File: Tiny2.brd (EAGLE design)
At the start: 30.1 x 64.9 mm, 13 parts

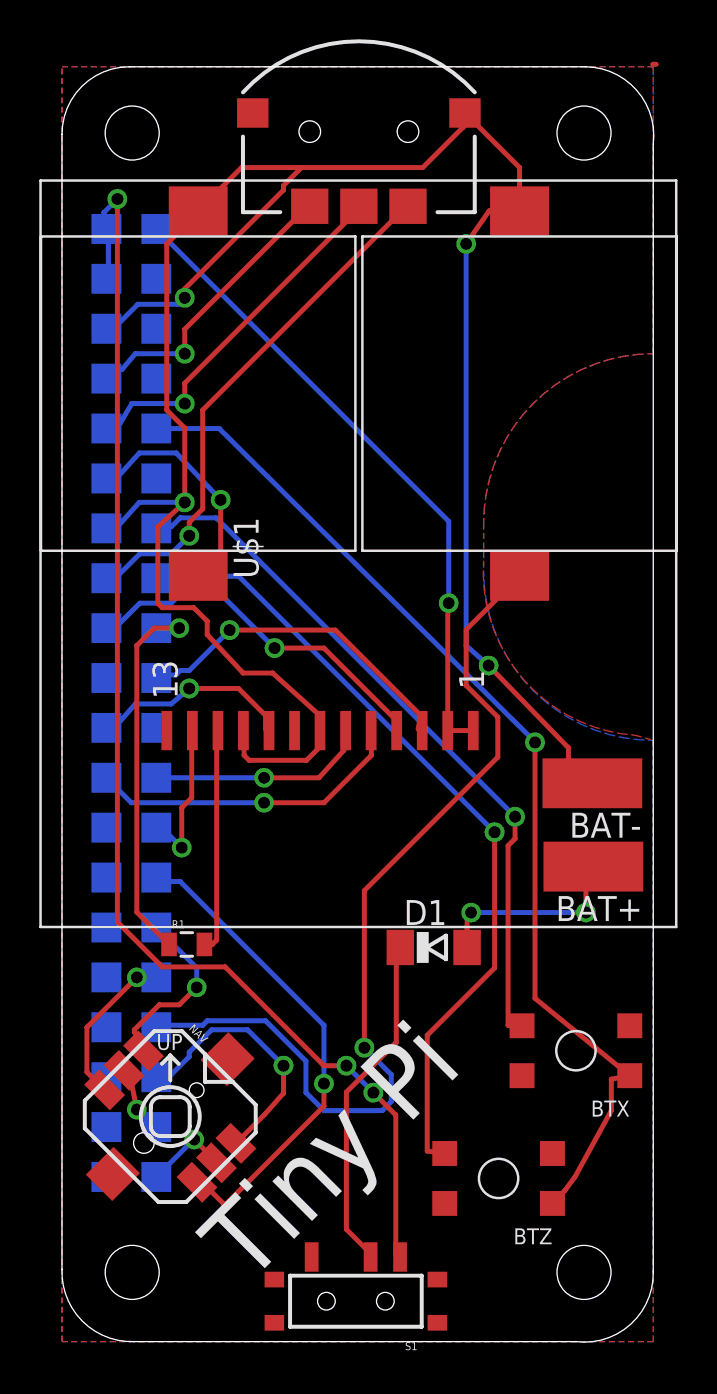
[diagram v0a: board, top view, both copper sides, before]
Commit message: removed diode, cleaned up some vias inside the header section
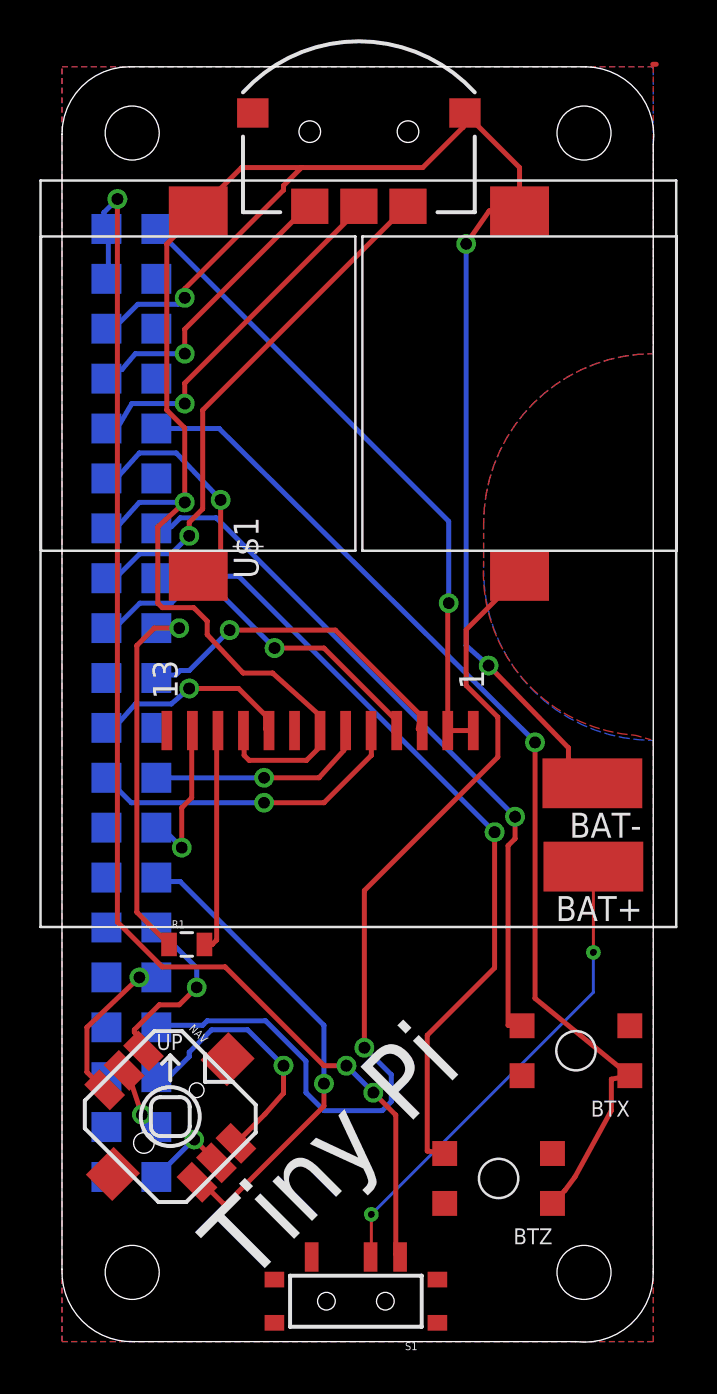
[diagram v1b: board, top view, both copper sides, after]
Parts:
- removed D1: PMLL4150, diode:SOD80C
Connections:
- removed net N$21: D1.C, S1.P
- net N$20: now also S1.P; no longer D1.A
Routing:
- net N$21: track 17.4 -> 0.00 mm
- net N$20: track 10.2 -> 24.6 mm
- net N$4: track 3.49 -> 4.12 mm
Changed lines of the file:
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@@
 <?xml version="1.0" encoding="utf-8"?>
 <!DOCTYPE eagle SYSTEM "eagle.dtd">
-<eagle version="8.1.0">
+<eagle version="8.3.2">
 <drawing>
 <settings>
 <setting alwaysvectorfont="no"/>
+<setting keepoldvectorfont="yes"/>
 <setting verticaltext="up"/>
 </settings>
@@
 <attribute name="PROD_ID" value="SWCH-08301" x="17.78" y="62.865" size="1.778" layer="27" display="off"/>
 </element>
-<element name="D1" library="diode" package="SOD80C" value="PMLL4150" x="21.59" y="21.336"/>
 </elements>
 <signals>
@@
 <contactref element="PI1" pad="37"/>
 <wire x1="7.4676" y1="12.192" x2="6.477" y2="13.0556" width="0.254" layer="16"/>
-<via x="6.477" y="13.081" extent="1-16" drill="0.6" alwaysstop="yes"/>
-<wire x1="6.477" y1="13.081" x2="6.223" y2="14.351" width="0.254" layer="1"/>
+<via x="6.731" y="12.827" extent="1-16" drill="0.6" alwaysstop="yes"/>
+<wire x1="6.731" y1="12.827" x2="6.223" y2="14.351" width="0.254" layer="1"/>
 <wire x1="6.223" y1="14.351" x2="5.878471875" y2="15.076528125" width="0.254" layer="1"/>
 <wire x1="5.878471875" y1="15.076528125" x2="5.82766875" y2="15.076528125" width="0.254" layer="1"/>
-<wire x1="6.477" y1="13.0556" x2="6.477" y2="13.081" width="0.254" layer="16"/>
+<wire x1="6.477" y1="13.0556" x2="6.731" y2="12.827" width="0.254" layer="16"/>
 </signal>
 <signal name="N$5">
@@
 <wire x1="4.83771875" y1="14.086578125" x2="3.937" y2="14.987296875" width="0.254" layer="1"/>
 <wire x1="3.937" y1="14.987296875" x2="3.937" y2="17.272" width="0.254" layer="1"/>
-<wire x1="3.937" y1="17.272" x2="6.477" y2="19.812" width="0.254" layer="1"/>
-<via x="6.477" y="19.812" extent="1-16" drill="0.6"/>
-<wire x1="6.477" y1="19.812" x2="7.4676" y2="19.812" width="0.254" layer="16"/>
+<wire x1="3.937" y1="17.272" x2="6.604" y2="19.812" width="0.254" layer="1"/>
+<via x="6.604" y="19.812" extent="1-16" drill="0.6"/>
+<wire x1="6.604" y1="19.812" x2="7.4676" y2="19.812" width="0.254" layer="16"/>
 </signal>
 <signal name="N$9">
@@
 <signal name="N$20">
 <contactref element="BAT+" pad="1"/>
-<contactref element="D1" pad="A"/>
-<wire x1="29.718" y1="25.4508" x2="29.337" y2="25.0698" width="0.254" layer="1"/>
-<wire x1="29.337" y1="25.0698" x2="29.337" y2="23.114" width="0.254" layer="1"/>
-<via x="29.337" y="23.114" extent="1-16" drill="0.6"/>
-<wire x1="29.337" y1="23.114" x2="23.495" y2="23.114" width="0.254" layer="16"/>
-<via x="23.495" y="23.114" extent="1-16" drill="0.6"/>
-<wire x1="23.495" y1="23.114" x2="23.29" y2="22.909" width="0.254" layer="1"/>
-<wire x1="23.29" y1="22.909" x2="23.29" y2="21.336" width="0.254" layer="1"/>
-</signal>
-<signal name="N$21">
-<contactref element="D1" pad="C"/>
 <contactref element="S1" pad="P"/>
-<wire x1="19.89" y1="21.336" x2="19.685" y2="20.623" width="0.254" layer="1"/>
-<wire x1="19.685" y1="20.623" x2="19.685" y2="16.51" width="0.254" layer="1"/>
-<wire x1="19.685" y1="16.51" x2="17.145" y2="13.97" width="0.254" layer="1"/>
-<wire x1="17.145" y1="13.97" x2="17.145" y2="6.985" width="0.254" layer="1"/>
-<wire x1="17.145" y1="6.985" x2="18.3776" y2="5.7524" width="0.254" layer="1"/>
-<wire x1="18.3776" y1="5.7524" x2="18.3776" y2="5.5774" width="0.254" layer="1"/>
+<wire x1="29.718" y1="25.4508" x2="29.718" y2="21.082" width="0.1524" layer="1"/>
+<via x="29.718" y="21.082" extent="1-16" drill="0.35"/>
+<wire x1="29.718" y1="21.082" x2="29.718" y2="19.05" width="0.1524" layer="16"/>
+<wire x1="29.718" y1="19.05" x2="18.415" y2="7.747" width="0.1524" layer="16"/>
+<via x="18.415" y="7.747" extent="1-16" drill="0.35"/>
+<wire x1="18.415" y1="7.747" x2="18.415" y2="5.6148" width="0.1524" layer="1"/>
+<wire x1="18.415" y1="5.6148" x2="18.3776" y2="5.5774" width="0.1524" layer="1"/>
 </signal>
 <signal name="3V3@1">
